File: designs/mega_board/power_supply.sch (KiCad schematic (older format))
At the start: 11 parts

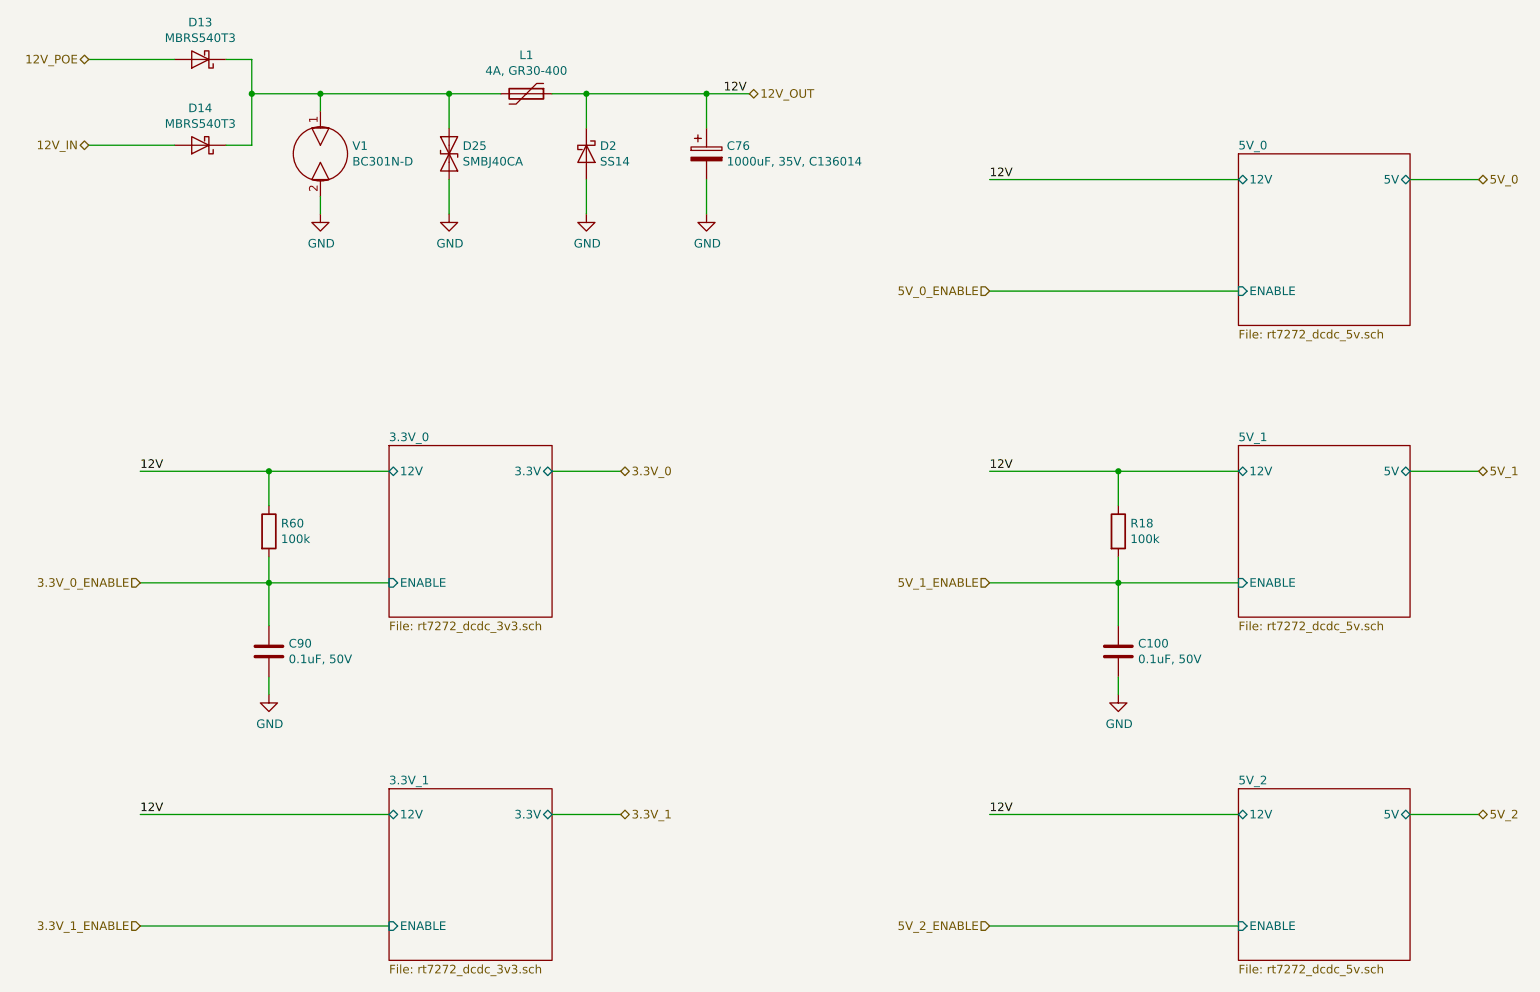
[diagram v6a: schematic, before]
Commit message: Add capacitor definito to BOM
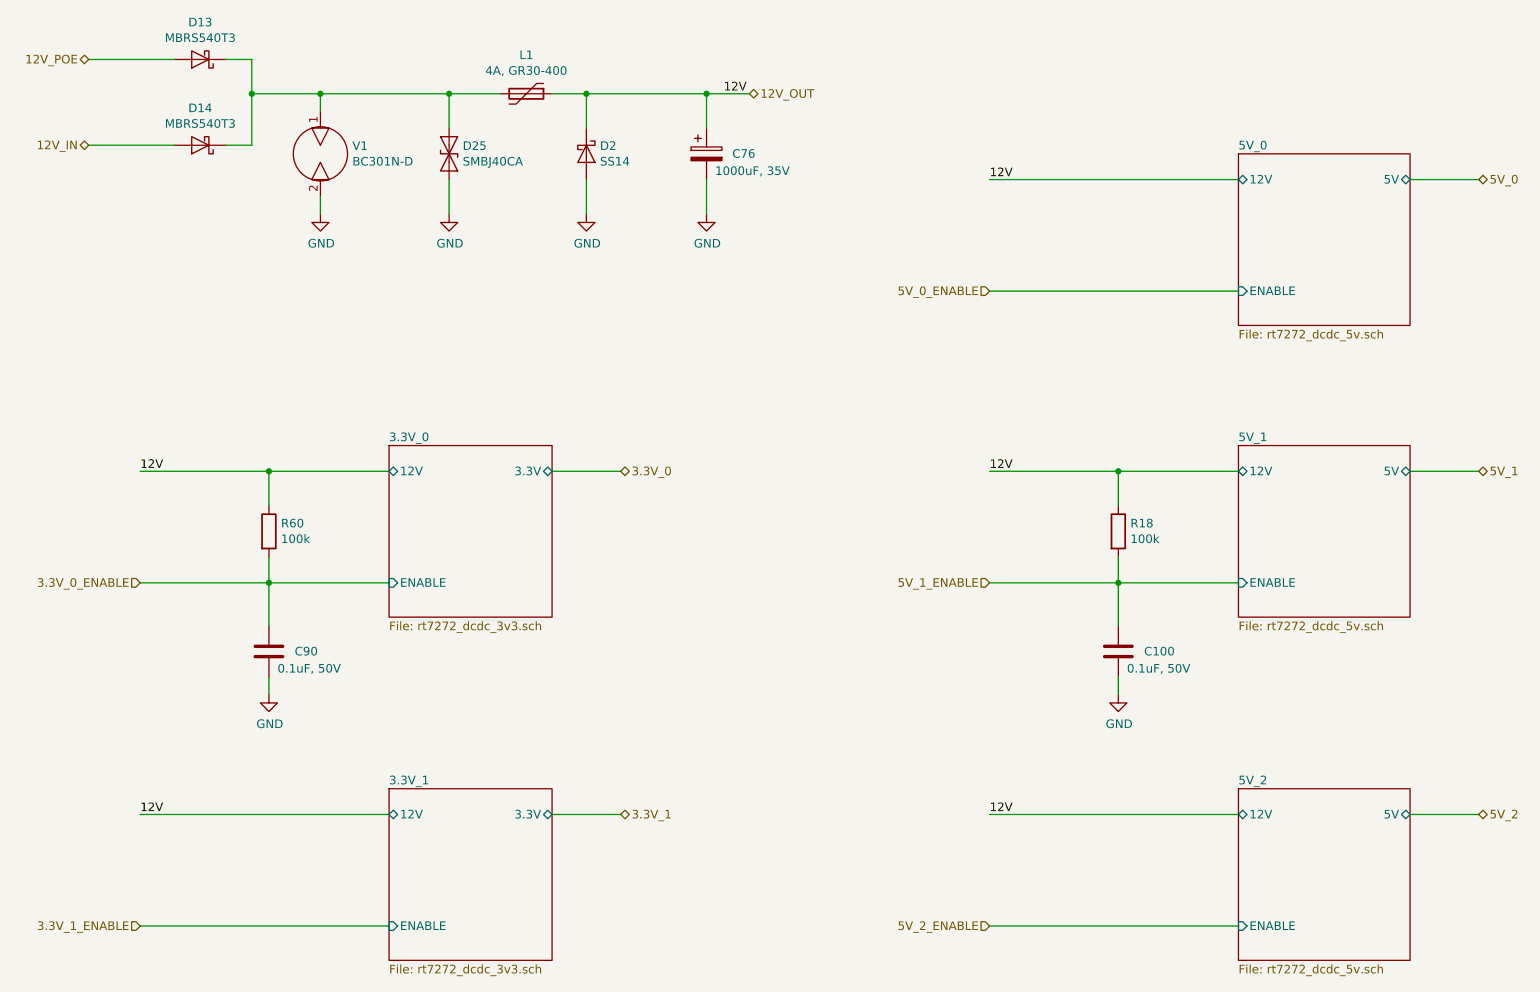
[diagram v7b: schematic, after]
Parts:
- C100, C90: Manufacturer (none) -> Murata Electronics; Manufacturer PN (none) -> GRM155R71H104KE14J; Supplier (none) -> DigiKey; Supplier PN (none) -> 490-13342-6-ND
- C76: value 1000uF, 35V, C136014 -> 1000uF, 35V; Manufacturer (none) -> Rubycon; Manufacturer PN (none) -> 35PX1000MEFC10X20; Supplier (none) -> DigiKey; Supplier PN (none) -> 1189-1745-ND
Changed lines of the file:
@@
 U 1 1 5D42F1FB
 P 2600 4350
-F 0 "C90" H 2715 4396 50  0000 L CNN
-F 1 "0.1uF, 50V" H 2715 4305 50  0000 L CNN
+F 0 "C90" H 2750 4350 50  0000 L CNN
+F 1 "0.1uF, 50V" H 2650 4250 50  0000 L CNN
 F 2 "LibreRouter_MegaBoard:C0402" H 2638 4200 50  0001 C CNN
 F 3 "~" H 2600 4350 50  0001 C CNN
+F 4 "DigiKey" H 2600 4350 50  0001 C CNN "Supplier"
+F 5 "Murata Electronics" H 2600 4350 50  0001 C CNN "Manufacturer"
+F 6 "GRM155R71H104KE14J" H 2600 4350 50  0001 C CNN "Manufacturer PN"
+F 7 "490-13342-6-ND" H 2600 4350 50  0001 C CNN "Supplier PN"
 	1    2600 4350
 	1    0    0    -1
@@
 U 1 1 5D4FE35A
 P 7550 4350
-F 0 "C100" H 7665 4396 50  0000 L CNN
-F 1 "0.1uF, 50V" H 7665 4305 50  0000 L CNN
+F 0 "C100" H 7700 4350 50  0000 L CNN
+F 1 "0.1uF, 50V" H 7600 4250 50  0000 L CNN
 F 2 "LibreRouter_MegaBoard:C0402" H 7588 4200 50  0001 C CNN
 F 3 "~" H 7550 4350 50  0001 C CNN
+F 4 "DigiKey" H 7550 4350 50  0001 C CNN "Supplier"
+F 5 "Murata Electronics" H 7550 4350 50  0001 C CNN "Manufacturer"
+F 6 "GRM155R71H104KE14J" H 7550 4350 50  0001 C CNN "Manufacturer PN"
+F 7 "490-13342-6-ND" H 7550 4350 50  0001 C CNN "Supplier PN"
 	1    7550 4350
 	1    0    0    -1
@@
 U 1 1 5D503338
 P 5150 1450
-F 0 "C76" H 5268 1496 50  0000 L CNN
-F 1 "1000uF, 35V, C136014" H 5268 1405 50  0000 L CNN
+F 0 "C76" H 5300 1450 50  0000 L CNN
+F 1 "1000uF, 35V" H 5200 1350 50  0000 L CNN
 F 2 "LibreRouter_MegaBoard:E3,5-10" H 5188 1300 50  0001 C CNN
 F 3 "~" H 5150 1450 50  0001 C CNN
+F 4 "DigiKey" H 5150 1450 50  0001 C CNN "Supplier"
+F 5 "Rubycon" H 5150 1450 50  0001 C CNN "Manufacturer"
+F 6 "35PX1000MEFC10X20" H 5150 1450 50  0001 C CNN "Manufacturer PN"
+F 7 "1189-1745-ND" H 5150 1450 50  0001 C CNN "Supplier PN"
 	1    5150 1450
 	1    0    0    -1

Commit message: Add BOM definition for almost all diodes
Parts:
- D13, D14: Manufacturer (none) -> ON Semiconductor; Manufacturer PN (none) -> MBRS540T3G; Supplier (none) -> DigiKey; Supplier PN (none) -> MBRS540T3GOSDKR-ND
- D2: Manufacturer (none) -> ON Semiconductor; Manufacturer PN (none) -> SS14; Supplier (none) -> DigiKey; Supplier PN (none) -> SS14CT-ND
- D25: Manufacturer (none) -> Littelfuse Inc.; Manufacturer PN (none) -> SMBJ40CA; Supplier (none) -> DigiKey; Supplier PN (none) -> SMBJ40CALFDKR-ND
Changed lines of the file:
@@
 F 2 "LibreRouter_MegaBoard:SMC" H 2200 900 50  0001 C CNN
 F 3 "~" H 2200 900 50  0001 C CNN
+F 4 "ON Semiconductor" H 2200 900 50  0001 C CNN "Manufacturer"
+F 5 "MBRS540T3G" H 2200 900 50  0001 C CNN "Manufacturer PN"
+F 6 "DigiKey" H 2200 900 50  0001 C CNN "Supplier"
+F 7 "MBRS540T3GOSDKR-ND" H 2200 900 50  0001 C CNN "Supplier PN"
 	1    2200 900
 	-1   0    0    1
@@
 F 2 "LibreRouter_MegaBoard:DO-214AA" H 3650 1450 50  0001 C CNN
 F 3 "~" H 3650 1450 50  0001 C CNN
+F 4 "Littelfuse Inc." H 3650 1450 50  0001 C CNN "Manufacturer"
+F 5 "SMBJ40CA" H 3650 1450 50  0001 C CNN "Manufacturer PN"
+F 6 "DigiKey" H 3650 1450 50  0001 C CNN "Supplier"
+F 7 "SMBJ40CALFDKR-ND" H 3650 1450 50  0001 C CNN "Supplier PN"
 	1    3650 1450
 	0    1    1    0
@@
 F 2 "LibreRouter_MegaBoard:DO214AC" H 4450 1450 50  0001 C CNN
 F 3 "~" H 4450 1450 50  0001 C CNN
+F 4 "ON Semiconductor" H 4450 1450 50  0001 C CNN "Manufacturer"
+F 5 "SS14" H 4450 1450 50  0001 C CNN "Manufacturer PN"
+F 6 "DigiKey" H 4450 1450 50  0001 C CNN "Supplier"
+F 7 "SS14CT-ND" H 4450 1450 50  0001 C CNN "Supplier PN"
 	1    4450 1450
 	0    1    1    0
@@
 F 2 "LibreRouter_MegaBoard:SMC" H 2200 1400 50  0001 C CNN
 F 3 "~" H 2200 1400 50  0001 C CNN
+F 4 "ON Semiconductor" H 2200 1400 50  0001 C CNN "Manufacturer"
+F 5 "MBRS540T3G" H 2200 1400 50  0001 C CNN "Manufacturer PN"
+F 6 "DigiKey" H 2200 1400 50  0001 C CNN "Supplier"
+F 7 "MBRS540T3GOSDKR-ND" H 2200 1400 50  0001 C CNN "Supplier PN"
 	1    2200 1400
 	-1   0    0    1
